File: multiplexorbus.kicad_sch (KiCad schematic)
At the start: 0 parts

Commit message: instantiate 3-8 decoders for MUX
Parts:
- added U? (x2): 74LS138, Package_DIP:DIP-16_W7.62mm, symbol 74xx:74LS138
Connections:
- new net +5V: U?.16 (VCC), U?.16 (VCC), U?.6 (E3)
- new net GND: U?.4 (E1), U?.4 (E1), U?.5 (E2), U?.8 (GND), U?.8 (GND)
- new net MUX_A0: U?.1 (A0), U?.1 (A0)
- new net MUX_A1: U?.2 (A1), U?.2 (A1)
- new net MUX_A2: U?.3 (A2), U?.3 (A2)
- new net MUX_A3: U?.5 (E2), U?.6 (E3)
- new net MUX_SEL_0: U?.15 (O0)
- new net MUX_SEL_1: U?.14 (O1)
- new net MUX_SEL_10: U?.13 (O2)
- new net MUX_SEL_11: U?.12 (O3)
- new net MUX_SEL_12: U?.11 (O4)
- new net MUX_SEL_13: U?.10 (O5)
- new net MUX_SEL_14: U?.9 (O6)
- new net MUX_SEL_15: U?.7 (O7)
- new net MUX_SEL_2: U?.13 (O2)
- new net MUX_SEL_3: U?.12 (O3)
- new net MUX_SEL_4: U?.11 (O4)
- new net MUX_SEL_5: U?.10 (O5)
- new net MUX_SEL_6: U?.9 (O6)
- new net MUX_SEL_7: U?.7 (O7)
- new net MUX_SEL_8: U?.15 (O0)
- new net MUX_SEL_9: U?.14 (O1)

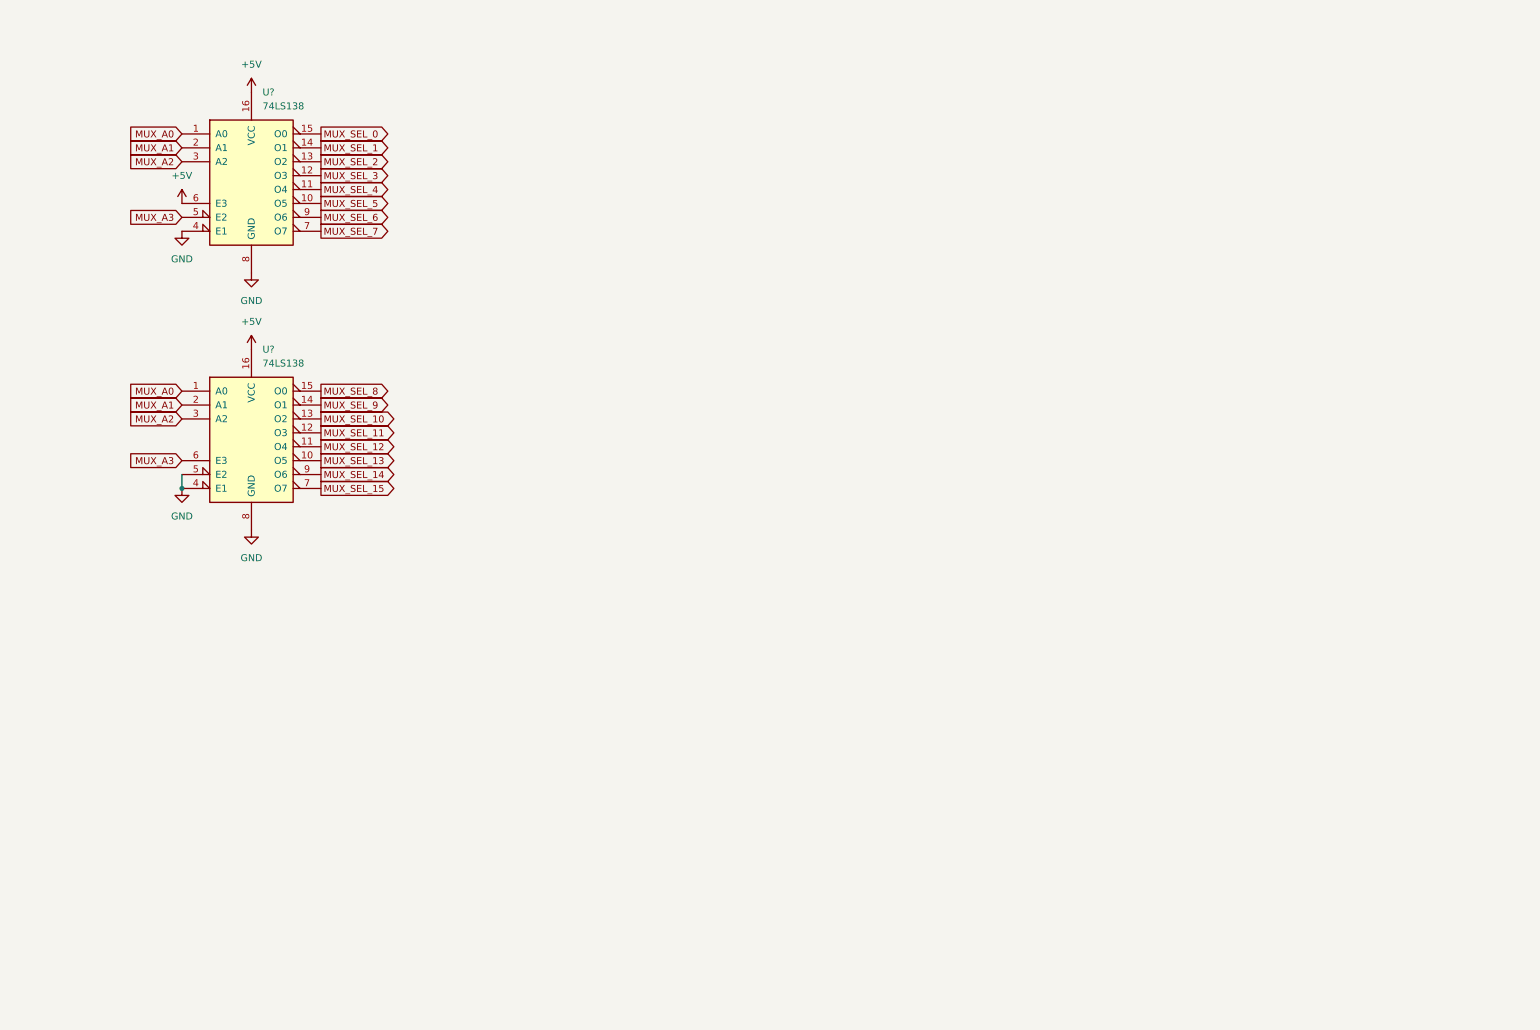
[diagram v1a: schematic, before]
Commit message: select latches for mux
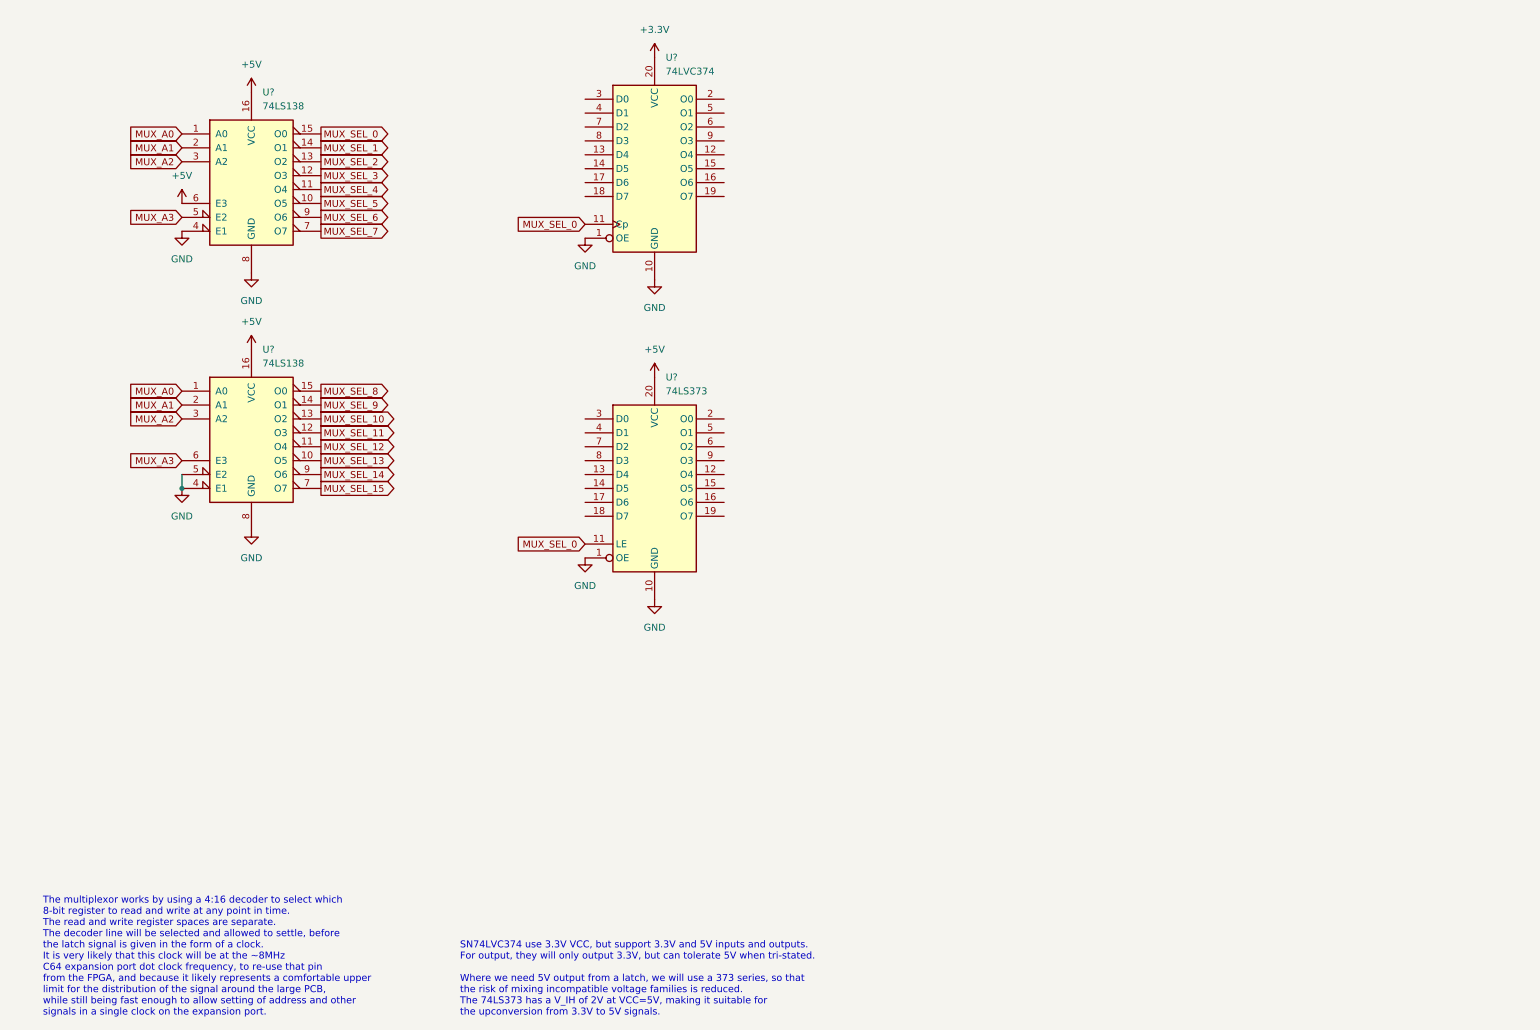
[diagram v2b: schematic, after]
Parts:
- added U?: 74LS373, Package_DIP:DIP-20_W7.62mm, symbol 74xx:74LS373
- added U?: 74LVC374, Package_DIP:DIP-20_W7.62mm, symbol 74xx:74HC374
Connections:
- net +5V: now also U?.20 (VCC)
- net GND: now also U?.1 (OE), U?.1 (OE), U?.10 (GND), U?.10 (GND)
- net MUX_SEL_0: now also U?.11 (Cp), U?.11 (LE)
- new net +3V3: U?.20 (VCC)
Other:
- note added: "SN74LVC374 use 3.3V VCC, but support 3.3V and 5V inputs and outputs. For output, they will only output 3.3V, but can tolerate 5V when tri-stated. Where we need 5V output from a latch, we will use a 373 series, so that the risk of mixing incompatible voltage families is reduced. The 74LS373 has a V_IH of 2V at VCC=5V, making it suitable for the upconversion from 3.3V to 5V signals."
- note added: "The multiplexor works by using a 4:16 decoder to select which 8-bit register to read and write at any point in time. The read and write register spaces are separate. The decoder line will be selected and allowed to settle, before the latch signal is given in the form of a clock. It is very likely that this clock will be at the ~8MHz C64 expansion port dot clock frequency, to re-use that pin from 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"
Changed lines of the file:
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@@
     (stroke (width 0) (type default) (color 0 0 0 0))
   )
+  (text "The multiplexor works by using a 4:16 decoder to select which\n8-bit register to read and write at any point in time.\nThe read and write register spaces are separate.\nThe decoder line will be selected and allowed to settle, before\nthe latch signal is given in the form of a clock.\nIt is very likely that this clock will be at the ~8MHz\nC64 expansion port dot clock frequency, to re-use that pin\nfrom the FPGA, and because it likely represents a comfortable upper\nlimit for the distribution of the signal around the large PCB,\nwhile still being fast enough to allow setting of address and other\nsignals in a single clock on the expansion port."
+    (at 15.24 194.31 0)
+    (effects (font (size 1.27 1.27)) (justify left bottom))
+  )
+  (text "SN74LVC374 use 3.3V VCC, but support 3.3V and 5V inputs and outputs.\nFor output, they will only output 3.3V, but can tolerate 5V when tri-stated.\n\nWhere we need 5V output from a latch, we will use a 373 series, so that\nthe risk of mixing incompatible voltage families is reduced.\nThe 74LS373 has a V_IH of 2V at VCC=5V, making it suitable for\nthe upconversion from 3.3V to 5V signals."
+    (at 91.44 194.31 0)
+    (effects (font (size 1.27 1.27)) (justify left bottom))
+  )
   (global_label "MUX_A0" (shape input) (at 40.64 33.02 180) (fields_autoplaced)
     (effects (font (size 1.27 1.27)) (justify right))
@@
     )
   )
+  (global_label "MUX_SEL_0" (shape input) (at 114.3 107.95 180) (fields_autoplaced)
+    (effects (font (size 1.27 1.27)) (justify right))
+    (property "Intersheet References" "${INTERSHEET_REFS}" (id 0) (at 101.364 107.8706 0)
+      (effects (font (size 1.27 1.27)) (justify right) hide)
+    )
+  )
   (global_label "MUX_SEL_4" (shape output) (at 66.04 43.18 0) (fields_autoplaced)
     (effects (font (size 1.27 1.27)) (justify left))
@@
     )
   )
+  (global_label "MUX_SEL_0" (shape input) (at 114.3 49.53 180) (fields_autoplaced)
+    (effects (font (size 1.27 1.27)) (justify right))
+    (property "Intersheet References" "${INTERSHEET_REFS}" (id 0) (at 101.364 49.4506 0)
+      (effects (font (size 1.27 1.27)) (justify right) hide)
+    )
+  )
   (global_label "MUX_A1" (shape input) (at 40.64 82.55 180) (fields_autoplaced)
     (effects (font (size 1.27 1.27)) (justify right))
@@
       (effects (font (size 1.27 1.27)) (justify left) hide)
     )
+  )
+  (symbol (lib_id "power:+5V") (at 127 77.47 0) (unit 1)
+    (in_bom yes) (on_board yes) (fields_autoplaced)
+    (property "Reference" "#PWR?" (id 0) (at 127 81.28 0)
+      (effects (font (size 1.27 1.27)) hide)
+    )
+    (property "Value" "+5V" (id 1) (at 127 72.39 0))
+    (property "Footprint" "" (id 2) (at 127 77.47 0)
+      (effects (font (size 1.27 1.27)) hide)
+    )
+    (property "Datasheet" "" (id 3) (at 127 77.47 0)
+      (effects (font (size 1.27 1.27)) hide)
+    )
+    (pin "1")
   )
   (symbol (lib_id "power:GND") (at 40.64 97.79 0) (unit 1)
@@
     (pin "1")
   )
+  (symbol (lib_id "power:GND") (at 127 118.11 0) (unit 1)
+    (in_bom yes) (on_board yes) (fields_autoplaced)
+    (property "Reference" "#PWR?" (id 0) (at 127 124.46 0)
+      (effects (font (size 1.27 1.27)) hide)
+    )
+    (property "Value" "GND" (id 1) (at 127 123.19 0))
+    (property "Footprint" "" (id 2) (at 127 118.11 0)
+      (effects (font (size 1.27 1.27)) hide)
+    )
+    (property "Datasheet" "" (id 3) (at 127 118.11 0)
+      (effects (font (size 1.27 1.27)) hide)
+    )
+    (pin "1")
+  )
+  (symbol (lib_id "power:GND") (at 114.3 52.07 0) (unit 1)
+    (in_bom yes) (on_board yes) (fields_autoplaced)
+    (property "Reference" "#PWR?" (id 0) (at 114.3 58.42 0)
+      (effects (font (size 1.27 1.27)) hide)
+    )
+    (property "Value" "GND" (id 1) (at 114.3 57.15 0))
+    (property "Footprint" "" (id 2) (at 114.3 52.07 0)
+      (effects (font (size 1.27 1.27)) hide)
+    )
+    (property "Datasheet" "" (id 3) (at 114.3 52.07 0)
+      (effects (font (size 1.27 1.27)) hide)
+    )
+    (pin "1")
+  )
+  (symbol (lib_id "74xx:74LS373") (at 127 97.79 0) (unit 1)
+    (in_bom yes) (on_board yes) (fields_autoplaced)
+    (property "Reference" "U?" (id 0) (at 129.0194 77.47 0)
+      (effects (font (size 1.27 1.27)) (justify left))
+    )
+    (property "Value" "74LS373" (id 1) (at 129.0194 80.01 0)
+      (effects (font (size 1.27 1.27)) (justify left))
+    )
+    (property "Footprint" "Package_DIP:DIP-20_W7.62mm" (id 2) (at 127 97.79 0)
+      (effects (font (size 1.27 1.27)) hide)
+    )
+    (property "Datasheet" "http://www.ti.com/lit/gpn/sn74LS373" (id 3) (at 127 97.79 0)
+      (effects (font (size 1.27 1.27)) hide)
+    )
+    (pin "1")
+    (pin "10")
+    (pin "11")
+    (pin "12")
+    (pin "13")
+    (pin "14")
+    (pin "15")
+    (pin "16")
+    (pin "17")
+    (pin "18")
+    (pin "19")
+    (pin "2")
+    (pin "20")
+    (pin "3")
+    (pin "4")
+    (pin "5")
+    (pin "6")
+    (pin "7")
+    (pin "8")
+    (pin "9")
+  )
   (symbol (lib_id "power:GND") (at 53.34 58.42 0) (unit 1)
     (in_bom yes) (on_board yes) (fields_autoplaced)
@@
     )
     (pin "1")
+  )
+  (symbol (lib_id "74xx:74HC374") (at 127 39.37 0) (unit 1)
+    (in_bom yes) (on_board yes) (fields_autoplaced)
+    (property "Reference" "U?" (id 0) (at 129.0194 19.05 0)
+      (effects (font (size 1.27 1.27)) (justify left))
+    )
+    (property "Value" "74LVC374" (id 1) (at 129.0194 21.59 0)
+      (effects (font (size 1.27 1.27)) (justify left))
+    )
+    (property "Footprint" "Package_DIP:DIP-20_W7.62mm" (id 2) (at 127 39.37 0)
+      (effects (font (size 1.27 1.27)) hide)
+    )
+    (property "Datasheet" "https://www.ti.com/lit/ds/symlink/cd74hct374.pdf" (id 3) (at 127 39.37 0)
+      (effects (font (size 1.27 1.27)) hide)
+    )
+    (pin "1")
+    (pin "10")
+    (pin "11")
+    (pin "12")
+    (pin "13")
+    (pin "14")
+    (pin "15")
+    (pin "16")
+    (pin "17")
+    (pin "18")
+    (pin "19")
+    (pin "2")
+    (pin "20")
+    (pin "3")
+    (pin "4")
+    (pin "5")
+    (pin "6")
+    (pin "7")
+    (pin "8")
+    (pin "9")
   )
   (symbol (lib_id "power:GND") (at 53.34 105.41 0) (unit 1)
@@
     (pin "9")
   )
+  (symbol (lib_id "power:GND") (at 127 59.69 0) (unit 1)
+    (in_bom yes) (on_board yes) (fields_autoplaced)
+    (property "Reference" "#PWR?" (id 0) (at 127 66.04 0)
+      (effects (font (size 1.27 1.27)) hide)
+    )
+    (property "Value" "GND" (id 1) (at 127 64.77 0))
+    (property "Footprint" "" (id 2) (at 127 59.69 0)
+      (effects (font (size 1.27 1.27)) hide)
+    )
+    (property "Datasheet" "" (id 3) (at 127 59.69 0)
+      (effects (font (size 1.27 1.27)) hide)
+    )
+    (pin "1")
+  )
   (symbol (lib_id "power:+5V") (at 40.64 45.72 0) (unit 1)
     (in_bom yes) (on_board yes) (fields_autoplaced)
@@
     )
     (property "Datasheet" "" (id 3) (at 40.64 45.72 0)
+      (effects (font (size 1.27 1.27)) hide)
+    )
+    (pin "1")
+  )
+  (symbol (lib_id "power:+3.3V") (at 127 19.05 0) (unit 1)
+    (in_bom yes) (on_board yes) (fields_autoplaced)
+    (property "Reference" "#PWR?" (id 0) (at 127 22.86 0)
+      (effects (font (size 1.27 1.27)) hide)
+    )
+    (property "Value" "+3.3V" (id 1) (at 127 13.97 0))
+    (property "Footprint" "" (id 2) (at 127 19.05 0)
+      (effects (font (size 1.27 1.27)) hide)
+    )
+    (property "Datasheet" "" (id 3) (at 127 19.05 0)
       (effects (font (size 1.27 1.27)) hide)
     )
@@
       (effects (font (size 1.27 1.27)) hide)
     )
+    (pin "1")
+  )
+  (symbol (lib_id "power:GND") (at 114.3 110.49 0) (unit 1)
+    (in_bom yes) (on_board yes) (fields_autoplaced)
+    (property "Reference" "#PWR?" (id 0) (at 114.3 116.84 0)
+      (effects (font (size 1.27 1.27)) hide)
+    )
+    (property "Value" "GND" (id 1) (at 114.3 115.57 0))
+    (property "Footprint" "" (id 2) (at 114.3 110.49 0)
+      (effects (font (size 1.27 1.27)) hide)
+    )
+    (property "Datasheet" "" (id 3) (at 114.3 110.49 0)
+      (effects (font (size 1.27 1.27)) hide)
+    )

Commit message: rework floppy buffers to use mux bus
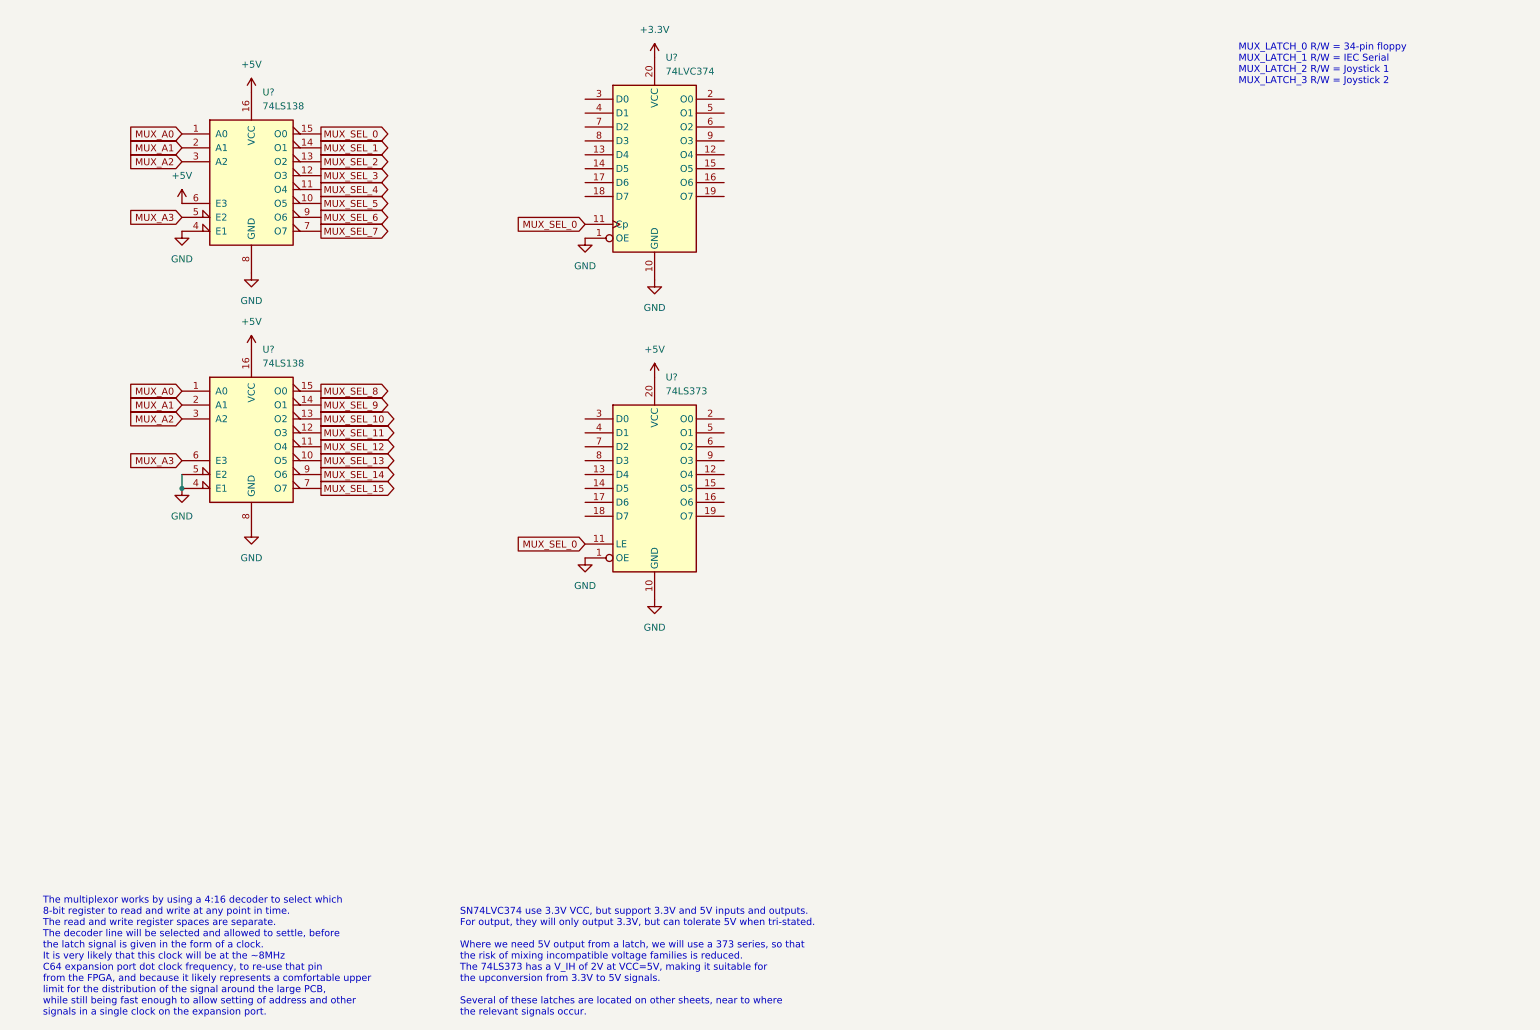
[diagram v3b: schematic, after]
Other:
- note added: "MUX_LATCH_0 R/W = 34-pin floppy MUX_LATCH_1 R/W = IEC Serial MUX_LATCH_2 R/W = Joystick 1 MUX_LATCH_3 R/W = Joystick 2"
- note added: "SN74LVC374 use 3.3V VCC, but support 3.3V and 5V inputs and outputs. For output, they will only output 3.3V, but can tolerate 5V when tri-stated. Where we need 5V output from a latch, we will use a 373 series, so that the risk of mixing incompatible voltage families is reduced. The 74LS373 has a V_IH of 2V at VCC=5V, making it suitable for the upconversion from 3.3V to 5V signals. Several of thes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"
- note removed: "SN74LVC374 use 3.3V VCC, but support 3.3V and 5V inputs and outputs. For output, they will only output 3.3V, but can tolerate 5V when tri-stated. Where we need 5V output from a latch, we will use a 373 series, so that the risk of mixing incompatible voltage families is reduced. The 74LS373 has a V_IH of 2V at VCC=5V, making it suitable for the upconversion from 3.3V to 5V signals."
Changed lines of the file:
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@@
     (effects (font (size 1.27 1.27)) (justify left bottom))
   )
-  (text "SN74LVC374 use 3.3V VCC, but support 3.3V and 5V inputs and outputs.\nFor output, they will only output 3.3V, but can tolerate 5V when tri-stated.\n\nWhere we need 5V output from a latch, we will use a 373 series, so that\nthe risk of mixing incompatible voltage families is reduced.\nThe 74LS373 has a V_IH of 2V at VCC=5V, making it suitable for\nthe upconversion from 3.3V to 5V signals."
+  (text "MUX_LATCH_0 R/W = 34-pin floppy\nMUX_LATCH_1 R/W = IEC Serial\nMUX_LATCH_2 R/W = Joystick 1\nMUX_LATCH_3 R/W = Joystick 2"
+    (at 233.68 24.13 0)
+    (effects (font (size 1.27 1.27)) (justify left bottom))
+  )
+  (text "SN74LVC374 use 3.3V VCC, but support 3.3V and 5V inputs and outputs.\nFor output, they will only output 3.3V, but can tolerate 5V when tri-stated.\n\nWhere we need 5V output from a latch, we will use a 373 series, so that\nthe risk of mixing incompatible voltage families is reduced.\nThe 74LS373 has a V_IH of 2V at VCC=5V, making it suitable for\nthe upconversion from 3.3V to 5V signals.\n\nSeveral of these latches are located on other sheets, near to where\nthe relevant signals occur."
     (at 91.44 194.31 0)
     (effects (font (size 1.27 1.27)) (justify left bottom))
